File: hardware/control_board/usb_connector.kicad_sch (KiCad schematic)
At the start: 6 parts, among them J6 USB4105-GF-A

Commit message: Adjust component values
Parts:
- J6: footprint (none) -> Local_Library:USB4105-GF-A
- R21, R22: footprint (none) -> Resistor_SMD:R_0603_1608Metric
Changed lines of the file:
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@@
   (junction (at 163.83 92.71) (diameter 0) (color 0 0 0 0)
   )
+  (junction (at 195.58 124.46) (diameter 0) (color 0 0 0 0)
+  )
+  (junction (at 175.26 104.14) (diameter 0) (color 0 0 0 0)
+  )
   (junction (at 175.26 99.06) (diameter 0) (color 0 0 0 0)
-  )
-  (junction (at 195.58 124.46) (diameter 0) (color 0 0 0 0)
-  )
-  (junction (at 175.26 104.14) (diameter 0) (color 0 0 0 0)
   )
   (no_connect (at 176.53 113.03))
@@
     (stroke (width 0) (type default))
   )
+  (wire (pts (xy 175.26 102.87) (xy 175.26 104.14))
+    (stroke (width 0) (type default))
+  )
+  (wire (pts (xy 163.83 92.71) (xy 163.83 93.98))
+    (stroke (width 0) (type default))
+  )
+  (wire (pts (xy 195.58 124.46) (xy 195.58 127))
+    (stroke (width 0) (type default))
+  )
+  (wire (pts (xy 175.26 77.47) (xy 175.26 78.74))
+    (stroke (width 0) (type default))
+  )
   (wire (pts (xy 175.26 104.14) (xy 175.26 105.41))
     (stroke (width 0) (type default))
   )
-  (wire (pts (xy 163.83 92.71) (xy 163.83 93.98))
-    (stroke (width 0) (type default))
-  )
-  (wire (pts (xy 195.58 124.46) (xy 195.58 127))
-    (stroke (width 0) (type default))
-  )
-  (wire (pts (xy 175.26 77.47) (xy 175.26 78.74))
-    (stroke (width 0) (type default))
-  )
   (wire (pts (xy 172.72 90.17) (xy 176.53 90.17))
     (stroke (width 0) (type default))
@@
     (stroke (width 0) (type default))
   )
+  (wire (pts (xy 120.65 99.06) (xy 121.92 99.06))
+    (stroke (width 0) (type default))
+  )
+  (wire (pts (xy 175.26 85.09) (xy 175.26 83.82))
+    (stroke (width 0) (type default))
+  )
+  (wire (pts (xy 167.64 90.17) (xy 163.83 90.17))
+    (stroke (width 0) (type default))
+  )
+  (wire (pts (xy 199.39 123.19) (xy 199.39 124.46))
+    (stroke (width 0) (type default))
+  )
   (wire (pts (xy 175.26 99.06) (xy 175.26 100.33))
     (stroke (width 0) (type default))
   )
-  (wire (pts (xy 120.65 99.06) (xy 121.92 99.06))
-    (stroke (width 0) (type default))
-  )
-  (wire (pts (xy 175.26 85.09) (xy 175.26 83.82))
-    (stroke (width 0) (type default))
-  )
-  (wire (pts (xy 167.64 90.17) (xy 163.83 90.17))
-    (stroke (width 0) (type default))
-  )
-  (wire (pts (xy 199.39 123.19) (xy 199.39 124.46))
-    (stroke (width 0) (type default))
-  )
   (wire (pts (xy 163.83 90.17) (xy 163.83 92.71))
     (stroke (width 0) (type default))
@@
   )
   (wire (pts (xy 175.26 100.33) (xy 176.53 100.33))
-    (stroke (width 0) (type default))
-  )
-  (wire (pts (xy 175.26 102.87) (xy 175.26 104.14))
     (stroke (width 0) (type default))
   )
@@
       (effects (font (size 1.27 1.27)))
     )
-    (property "Footprint" "" (at 170.18 92.71 0)
+    (property "Footprint" "Resistor_SMD:R_0603_1608Metric" (at 170.18 92.71 0)
       (effects (font (size 1.27 1.27)) hide)
     )
@@
       (effects (font (size 1.27 1.27)))
     )
-    (property "Footprint" "" (at 170.18 90.17 0)
+    (property "Footprint" "Resistor_SMD:R_0603_1608Metric" (at 170.18 90.17 0)
       (effects (font (size 1.27 1.27)) hide)
     )
@@
       (effects (font (size 1.27 1.27)) (justify left))
     )
-    (property "Footprint" "" (at 187.96 100.33 0)
-      (effects (font (size 1.27 1.27)) hide)
-    )
+    (property "Footprint" "Local_Library:USB4105-GF-A" (at 187.96 100.33 0)
+      (effects (font (size 1.27 1.27)) hide)
+    )

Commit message: Assign footprints to components
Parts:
- removed U?: USBLC6-2P6, Package_TO_SOT_SMD:SOT-666, symbol Power_Protection:USBLC6-2P6
- added U4: USBLC6-2SC6, Package_TO_SOT_SMD:SOT-23-6, symbol Power_Protection:USBLC6-2SC6
- J6: value USB4105-GF-A -> USB_C; Component (none) -> USB4105-GF-A
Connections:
- net +5V: now also U4.5 (VBUS)
- net D+: now also U4.6 (I/O1)
- net D-: now also U4.4 (I/O2)
- net DATA+: now also U4.1 (I/O1)
- net DATA-: now also U4.3 (I/O2)
- net GND: now also U4.2 (GND)
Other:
- moved on the sheet: C2, FB4, J6, R21, R22

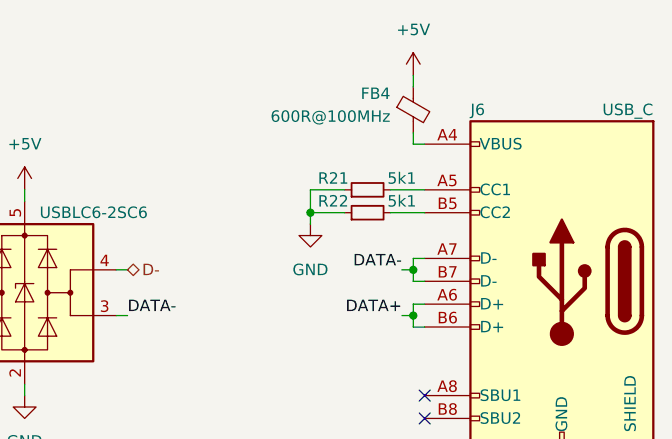
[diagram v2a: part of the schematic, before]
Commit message: Place components on the control board PCB
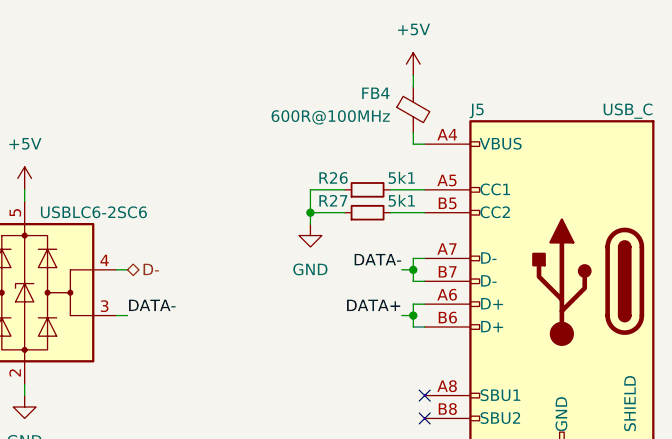
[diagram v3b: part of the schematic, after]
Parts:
- J5: renamed from J6; footprint Local_Library:USB4105-GF-A -> Connector_USB:USB_C_Receptacle_GCT_USB4105-xx-A_16P_TopMnt_Horizontal
- renumbered R21 to R26, R22 to R27
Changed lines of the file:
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@@
+        )
+        (path "/b652b05a-4e3d-4ad1-b032-18886abe7d45/3d0d4351-20fe-44b0-a348-a3114badfe96"
+          (reference "#PWR061") (unit 1)
+        )
+      )
+    )
+  )
+  (symbol (lib_id "power:GND") (at 196.85 127 0) (mirror y) (unit 1)
+    (in_bom yes) (on_board yes) (dnp no)
+    (property "Reference" "#PWR?" (at 196.85 133.35 0)
+      (effects (font (size 1.27 1.27)) hide)
+    )
+    (property "Value" "GND" (at 196.85 132.08 0)
+      (effects (font (size 1.27 1.27)))
+    )
+    (property "Footprint" "" (at 196.85 127 0)
+      (effects (font (size 1.27 1.27)) hide)
+    )
+    (property "Datasheet" "" (at 196.85 127 0)
+      (effects (font (size 1.27 1.27)) hide)
+    )
+    (pin "1")
+    (instances
+      (project "control_board"
+        (path "/b652b05a-4e3d-4ad1-b032-18886abe7d45"
+          (reference "#PWR?") (unit 1)
+        )
+        (path "/b652b05a-4e3d-4ad1-b032-18886abe7d45/02711725-e382-48ba-bf33-23fe46c66e66"
+          (reference "#PWR023") (unit 1)
         )
         (path "/b652b05a-4e3d-4ad1-b032-18886abe7d45/3d0d4351-20fe-44b0-a348-a3114badfe96"
@@
     )
   )
-  (symbol (lib_id "power:GND") (at 196.85 127 0) (mirror y) (unit 1)
-    (in_bom yes) (on_board yes) (dnp no)
-    (property "Reference" "#PWR?" (at 196.85 133.35 0)
-      (effects (font (size 1.27 1.27)) hide)
-    )
-    (property "Value" "GND" (at 196.85 132.08 0)
-      (effects (font (size 1.27 1.27)))
-    )
-    (property "Footprint" "" (at 196.85 127 0)
-      (effects (font (size 1.27 1.27)) hide)
-    )
-    (property "Datasheet" "" (at 196.85 127 0)
-      (effects (font (size 1.27 1.27)) hide)
-    )
-    (pin "1")
-    (instances
-      (project "control_board"
-        (path "/b652b05a-4e3d-4ad1-b032-18886abe7d45"
-          (reference "#PWR?") (unit 1)
-        )
-        (path "/b652b05a-4e3d-4ad1-b032-18886abe7d45/02711725-e382-48ba-bf33-23fe46c66e66"
-          (reference "#PWR023") (unit 1)
-        )
-        (path "/b652b05a-4e3d-4ad1-b032-18886abe7d45/3d0d4351-20fe-44b0-a348-a3114badfe96"
-          (reference "#PWR065") (unit 1)
-        )
-      )
-    )
-  )
   (symbol (lib_id "power:+5V") (at 176.53 77.47 0) (mirror y) (unit 1)
     (in_bom yes) (on_board yes) (dnp no)
@@
         )
         (path "/b652b05a-4e3d-4ad1-b032-18886abe7d45/3d0d4351-20fe-44b0-a348-a3114badfe96"
-          (reference "#PWR064") (unit 1)
+          (reference "#PWR062") (unit 1)
         )
       )
@@
         )
         (path "/b652b05a-4e3d-4ad1-b032-18886abe7d45/3d0d4351-20fe-44b0-a348-a3114badfe96"
-          (reference "#PWR060") (unit 1)
+          (reference "#PWR058") (unit 1)
         )
       )
@@
   (symbol (lib_id "Device:R_Small") (at 171.45 92.71 90) (unit 1)
     (in_bom yes) (on_board yes) (dnp no)
-    (property "Reference" "R22" (at 167.64 91.44 90)
+    (property "Reference" "R27" (at 167.64 91.44 90)
       (effects (font (size 1.27 1.27)))
     )
@@
       (project "control_board"
         (path "/b652b05a-4e3d-4ad1-b032-18886abe7d45/3d0d4351-20fe-44b0-a348-a3114badfe96"
-          (reference "R22") (unit 1)
+          (reference "R27") (unit 1)
         )
       )
@@
   (symbol (lib_id "Device:R_Small") (at 171.45 90.17 90) (unit 1)
     (in_bom yes) (on_board yes) (dnp no)
-    (property "Reference" "R21" (at 167.64 88.9 90)
+    (property "Reference" "R26" (at 167.64 88.9 90)
       (effects (font (size 1.27 1.27)))
     )
@@
       (project "control_board"
         (path "/b652b05a-4e3d-4ad1-b032-18886abe7d45/3d0d4351-20fe-44b0-a348-a3114badfe96"
-          (reference "R21") (unit 1)
+          (reference "R26") (unit 1)
         )
       )
@@
         )
         (path "/b652b05a-4e3d-4ad1-b032-18886abe7d45/3d0d4351-20fe-44b0-a348-a3114badfe96"
-          (reference "C20") (unit 1)
+          (reference "C18") (unit 1)
         )
       )
@@
         )
         (path "/b652b05a-4e3d-4ad1-b032-18886abe7d45/3d0d4351-20fe-44b0-a348-a3114badfe96"
-          (reference "#PWR061") (unit 1)
+          (reference "#PWR059") (unit 1)
         )
       )
@@
         )
         (path "/b652b05a-4e3d-4ad1-b032-18886abe7d45/3d0d4351-20fe-44b0-a348-a3114badfe96"
-          (reference "#PWR059") (unit 1)
+          (reference "#PWR057") (unit 1)
         )
       )
@@
   (symbol (lib_id "Connector:USB_C_Receptacle_USB2.0") (at 193.04 100.33 0) (mirror y) (unit 1)
     (in_bom yes) (on_board yes) (dnp no)
-    (property "Reference" "J6" (at 182.88 81.28 0)
+    (property "Reference" "J5" (at 182.88 81.28 0)
       (effects (font (size 1.27 1.27)) (justify right))
     )
@@
       (effects (font (size 1.27 1.27)) (justify left))
     )
-    (property "Footprint" "Local_Library:USB4105-GF-A" (at 189.23 100.33 0)
+    (property "Footprint" "Connector_USB:USB_C_Receptacle_GCT_USB4105-xx-A_16P_TopMnt_Horizontal" (at 189.23 100.33 0)
       (effects (font (size 1.27 1.27)) hide)
     )
@@
       (project "control_board"
         (path "/b652b05a-4e3d-4ad1-b032-18886abe7d45/3d0d4351-20fe-44b0-a348-a3114badfe96"
-          (reference "J6") (unit 1)
+          (reference "J5") (unit 1)
         )
       )
@@
         )
         (path "/b652b05a-4e3d-4ad1-b032-18886abe7d45/3d0d4351-20fe-44b0-a348-a3114badfe96"
-          (reference "#PWR062") (unit 1)
-        )
-      )
+          (reference "#PWR060") (unit 1)
+        )
+      )

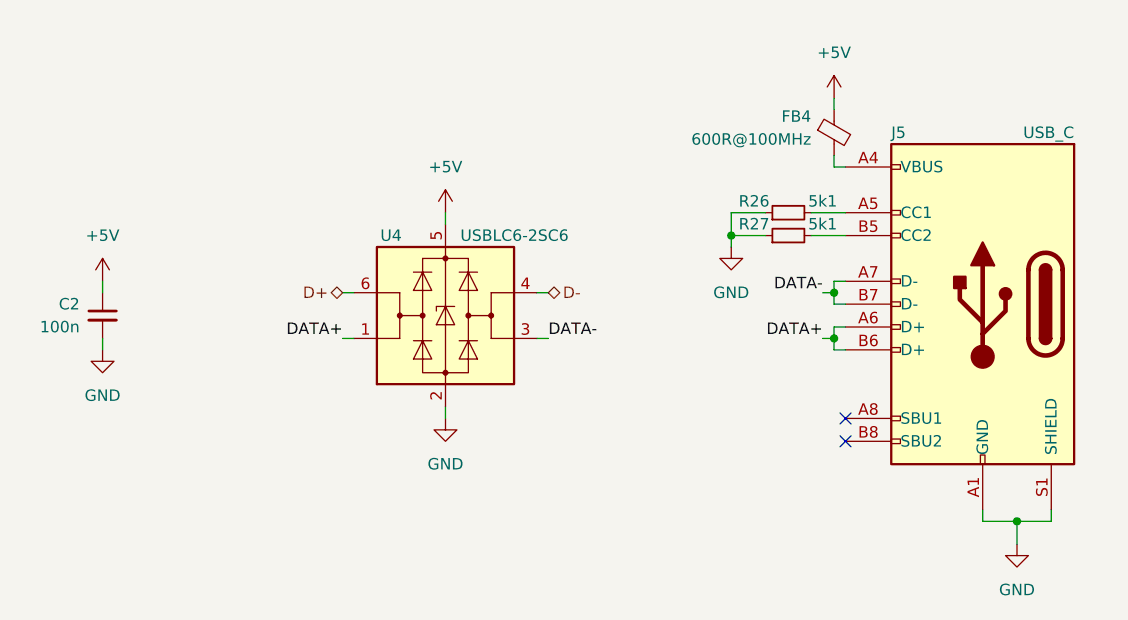
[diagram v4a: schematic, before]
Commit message: Route control board PCB tracks
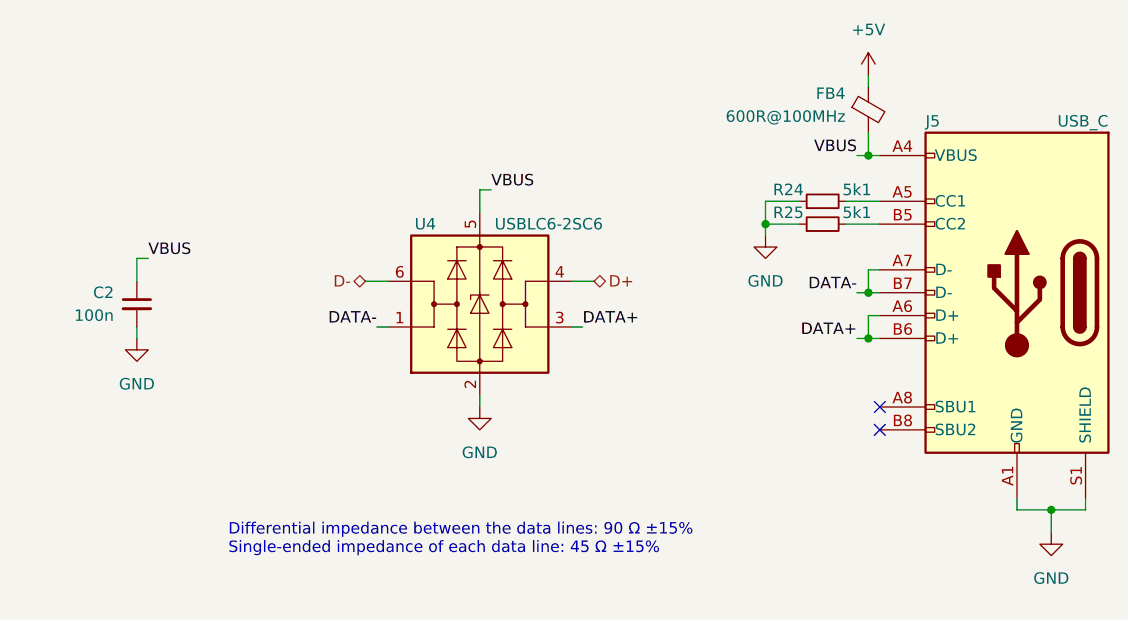
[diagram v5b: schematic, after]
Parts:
- renumbered R26 to R24, R27 to R25
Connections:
- net +5V: no longer C2.1, U4.5 (VBUS)
- net D+: now also U4.4 (I/O2); no longer U4.6 (I/O1)
- net D-: now also U4.6 (I/O1); no longer U4.4 (I/O2)
- net DATA+: now also U4.3 (I/O2); no longer U4.1 (I/O1)
- net DATA-: now also U4.1 (I/O1); no longer U4.3 (I/O2)
- net VBUS: now reaches FB4.2, J5.A4 (VBUS), J5.A9 (VBUS), J5.B4 (VBUS), J5.B9 (VBUS)
- net VBUS: now also C2.1, U4.5 (VBUS)
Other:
- note added: "Differential impedance between the data lines: 90 Ω ±15% Single-ended impedance of each data line: 45 Ω ±15%"
- moved on the sheet: C2, FB4, J5, R24, R25, U4

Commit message: Minor layout adjustments
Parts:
- FB4: value 600R@100MHz -> 470R@100MHz
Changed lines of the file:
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@@
       (effects (font (size 1.27 1.27)) (justify right top))
     )
-    (property "Value" "600R@100MHz" (at 177.8 78.74 0)
+    (property "Value" "470R@100MHz" (at 177.8 78.74 0)
       (effects (font (size 1.27 1.27)) (justify right top))
     )

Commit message: Cleanup the project
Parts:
- FB4: value 470R@100MHz -> 470R
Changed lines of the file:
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@@
       (effects (font (size 1.27 1.27)) (justify right top))
     )
-    (property "Value" "470R@100MHz" (at 177.8 78.74 0)
+    (property "Value" "470R" (at 177.8 78.74 0)
       (effects (font (size 1.27 1.27)) (justify right top))
     )
